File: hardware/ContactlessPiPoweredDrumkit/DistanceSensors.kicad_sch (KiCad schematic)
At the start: 36 parts, among them J2 Conn_01x06_Socket, J3 Conn_01x06_Socket, J4 Conn_01x06_Socket, J5 Conn_01x06_Socket, J6 Conn_01x06_Socket, J7 Conn_01x06_Socket, U1 VL53L4CD, U2 VL53L4CD, U3 VL53L4CD, U4 VL53L4CD, U5 VL53L4CD, U6 VL53L4CD

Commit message: Commit missed items
Missed a few items
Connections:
- net +3.3V: no longer U4.1 (AVDDVCSEL)
- net D4_GPIO1: no longer U4.7 (GPIO1)
- net D4_XSHUT: no longer U4.5 (XSHUT)
- net GND: no longer U4.3 (GND)
- net I2C0_SCL: no longer U4.10 (SCL)
- net I2C0_SDA: no longer U4.9 (SDA)
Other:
- moved on the sheet: U4
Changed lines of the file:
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@@
     )
   )
-  (symbol (lib_id "ContactlessPPD_custom_lib:VL53L4CD") (at 188.595 102.87 0) (unit 1)
+  (symbol (lib_id "ContactlessPPD_custom_lib:VL53L4CD") (at 188.595 102.87 0) (mirror y) (unit 1)
     (in_bom yes) (on_board yes) (dnp no)
-    (property "Reference" "U4" (at 196.977 114.808 0)
+    (property "Reference" "U4" (at 180.213 114.808 0)
       (effects (font (size 1.27 1.27)) (justify left))
     )
-    (property "Value" "VL53L4CD" (at 197.231 116.84 0)
+    (property "Value" "VL53L4CD" (at 179.959 116.84 0)
       (effects (font (size 1.27 1.27)) (justify left))
     )
-    (property "Footprint" "Sensor_Distance:ST_VL53L1x" (at 208.915 116.84 0)
+    (property "Footprint" "Sensor_Distance:ST_VL53L1x" (at 168.275 116.84 0)
       (effects (font (size 1.27 1.27)) hide)
     )
-    (property "Datasheet" "https://www.st.com/resource/en/datasheet/VL53L4CD.pdf" (at 191.135 100.33 0)
+    (property "Datasheet" "https://www.st.com/resource/en/datasheet/VL53L4CD.pdf" (at 186.055 100.33 0)
       (effects (font (size 1.27 1.27)) hide)
     )

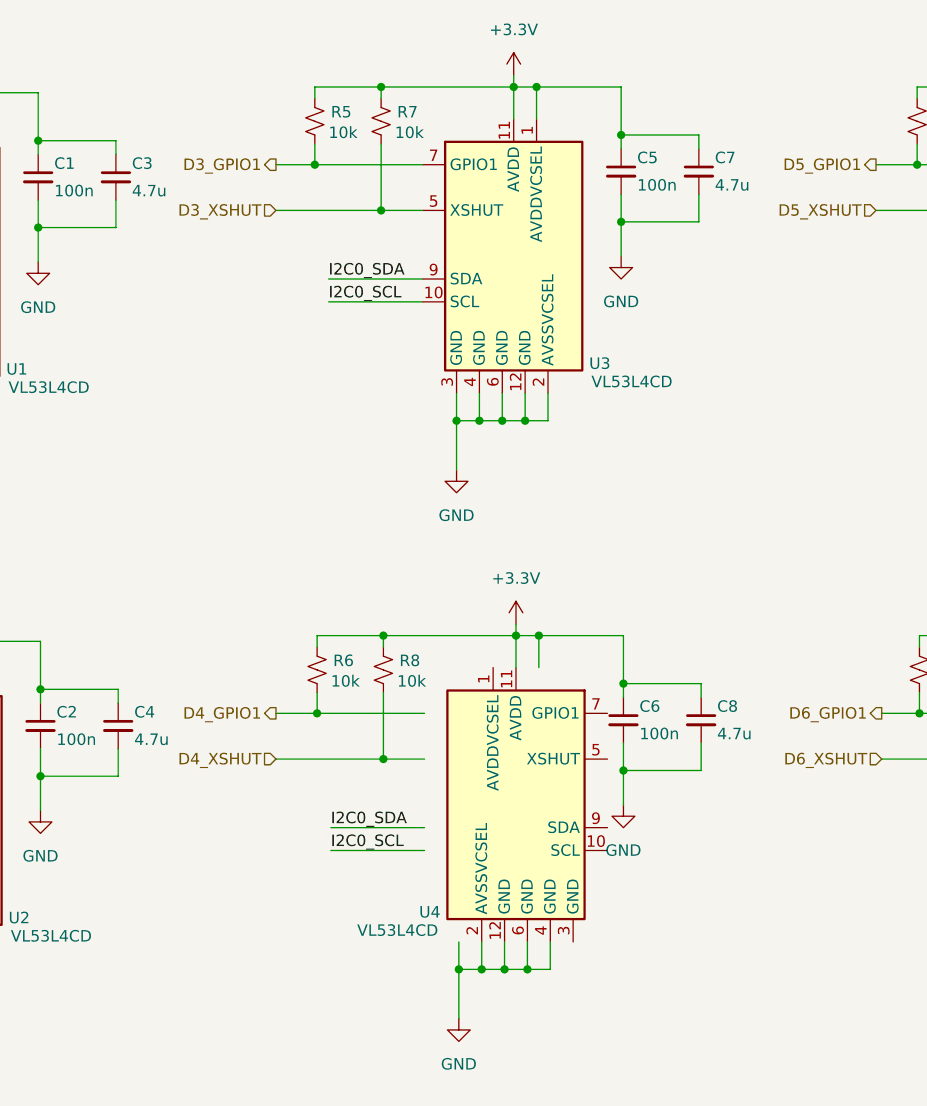
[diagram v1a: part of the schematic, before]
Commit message: Reviewed PCB DRC
Reduced constraint size from .3mm to .25mm
Move pullup resistors slightly
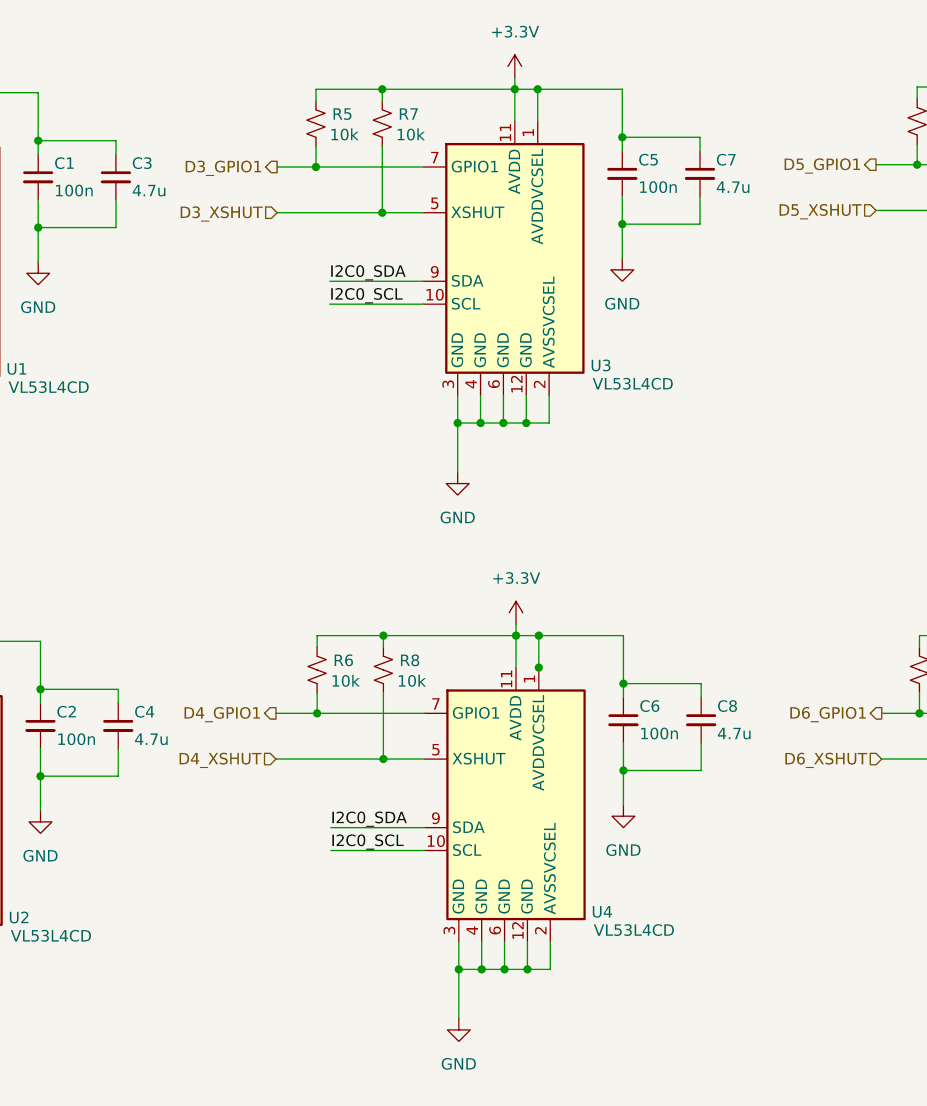
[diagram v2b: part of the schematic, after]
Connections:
- net +3.3V: now also U4.1 (AVDDVCSEL)
- net D4_GPIO1: now also U4.7 (GPIO1)
- net D4_XSHUT: now also U4.5 (XSHUT)
- net GND: now also U4.3 (GND)
- net I2C0_SCL: now also U4.10 (SCL)
- net I2C0_SDA: now also U4.9 (SDA)
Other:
- moved on the sheet: U4
